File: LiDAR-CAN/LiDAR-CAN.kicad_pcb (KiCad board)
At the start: 4 copper layers, 60 x 55 mm, 137 parts, among them J1 XT30(2+2), J2 XT30(2+2), J3 G7LX-A88S7-BP-G/Y, J4 XT30(2+2), J5 61300511121, SW1 RST, U1 LMR51430, U2 LMR51430, U3 W5500, U4 TCAN4550RGY, U5 STM32F401RBT6, Y1 25MHz, Y2 40MHz, Y3 25MHz

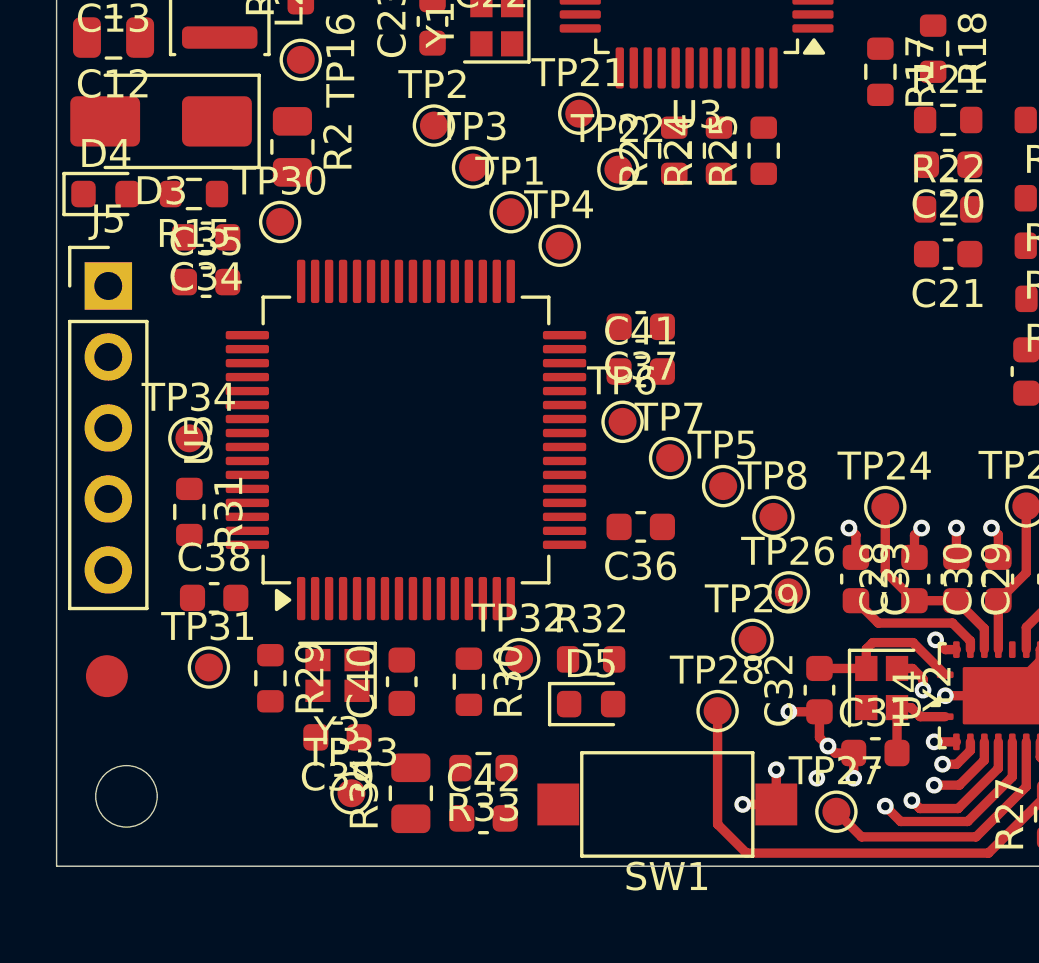
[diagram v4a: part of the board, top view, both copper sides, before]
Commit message: Add MCU routing
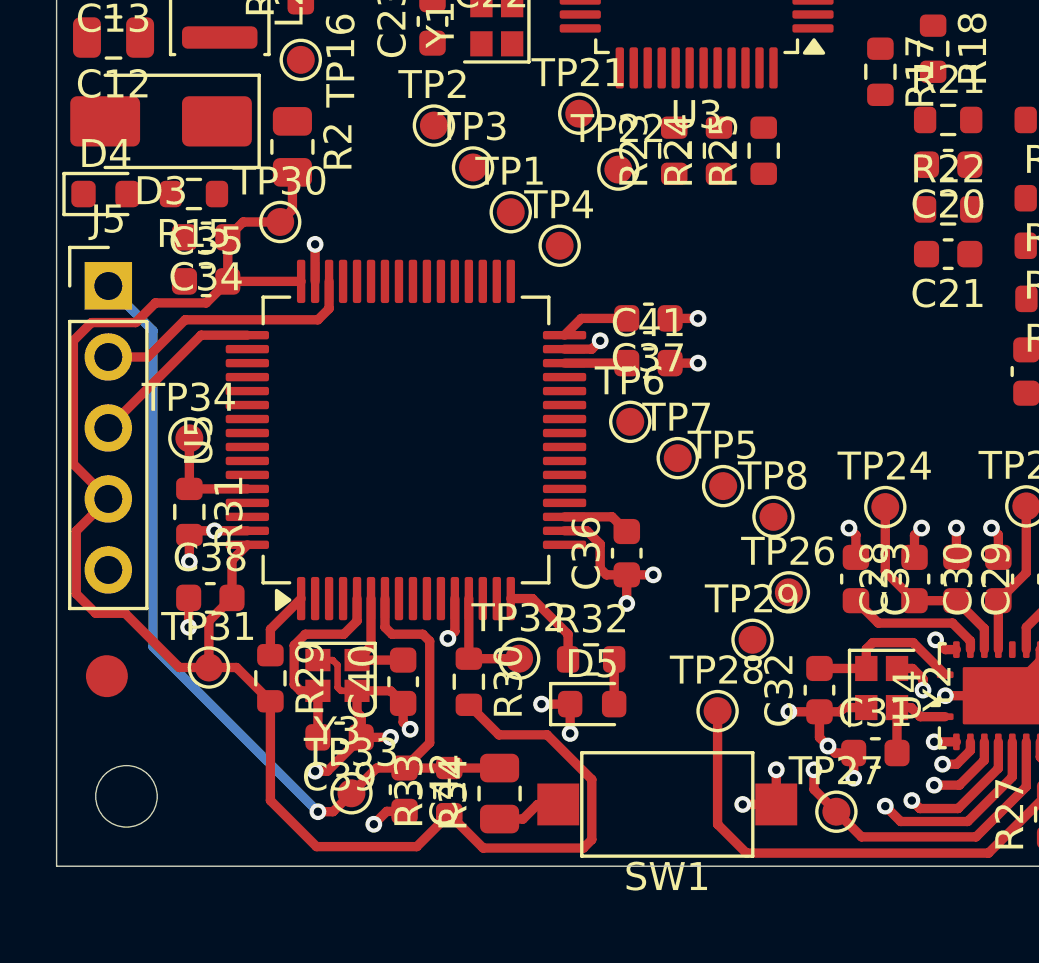
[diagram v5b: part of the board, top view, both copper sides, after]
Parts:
- moved R34 3.18 mm to (135.8, 117.4)
- moved C42 3.01 mm to (132.4, 117.3), turned to -90 degrees
- moved R33 1.48 mm to (134.1, 117.3), turned to 90 degrees
- moved C36 1.06 mm to (140.4, 108.8), turned to 90 degrees
- moved C37 0.41 mm to (141.2, 100.4)
- moved C41 0.41 mm to (141.2, 102.0)
- moved TP6 0.28 mm to (140.5, 104.1)
- moved TP7 0.28 mm to (142.2, 105.4)
- moved C38 0.14 mm to (125.5, 110.4)
- moved C39 0.07 mm to (130.1, 115.4)
- moved C40 0.05 mm to (132.4, 113.4)
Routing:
- net +3.3V: track 7.45 -> 75.1 mm
- net /Microcontroller/MCU_RST: track 0.00 -> 36.8 mm, vias 0 -> 1
- net GND: track 31.3 -> 62.0 mm, vias 17 -> 33
- net /Microcontroller/SWDIO: track 0.00 -> 9.59 mm
- net /Microcontroller/OSC_IN: track 0.00 -> 7.42 mm
- net /Microcontroller/SWCLK: track 0.00 -> 6.35 mm
- net /Microcontroller/OSC_OUT: track 0.00 -> 4.06 mm
- net /Microcontroller/VREF+: track 0.00 -> 3.95 mm
- net /Microcontroller/BOOT0: track 0.00 -> 3.89 mm
- net /Microcontroller/ULED: track 0.00 -> 3.48 mm
- net Net-(U5-VBAT): track 0.00 -> 2.48 mm
- net Net-(R34-Pad1): track 0.00 -> 2.32 mm
- net Net-(U5-VCAP1): track 0.00 -> 1.95 mm
- net /CAN Interface/~{CS}: track 9.52 -> 11.3 mm, vias 0 -> 1
- net Net-(D5-A): track 0.00 -> 1.60 mm
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
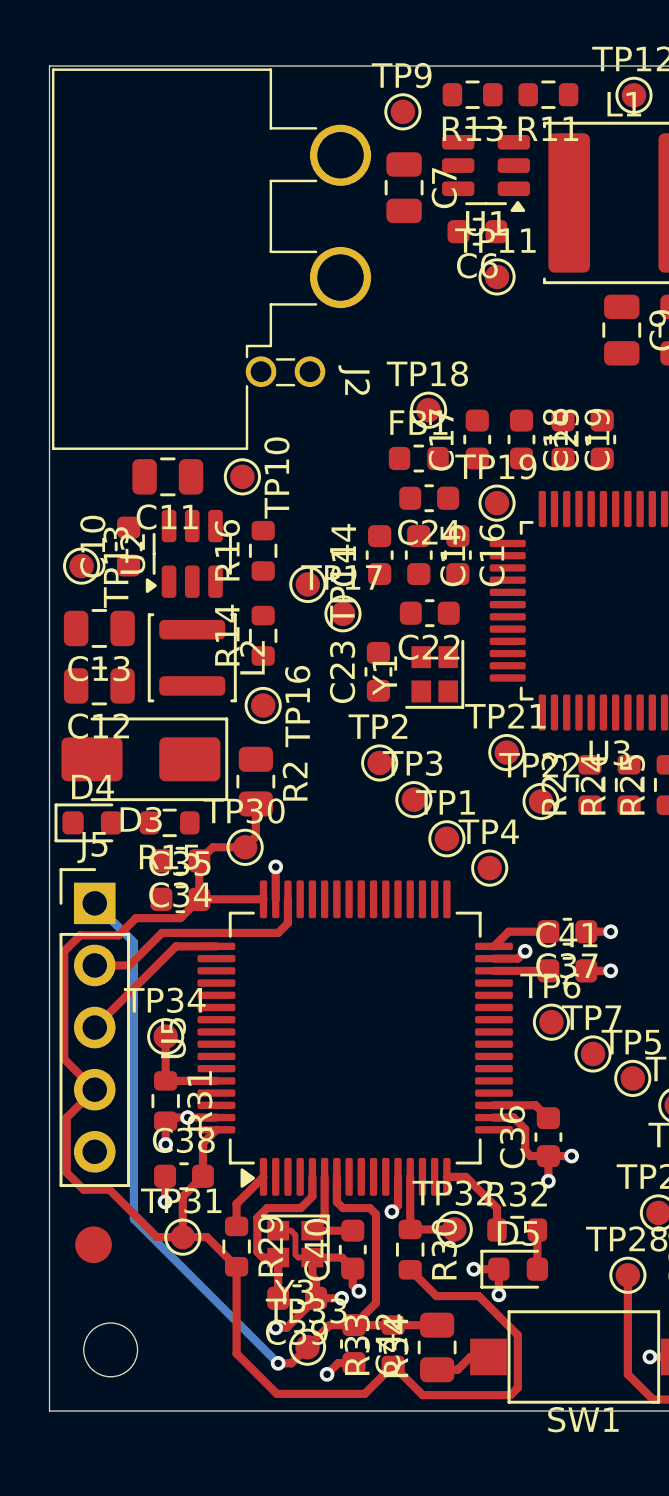
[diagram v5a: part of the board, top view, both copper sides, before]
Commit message: Add 3.3V regulator routing
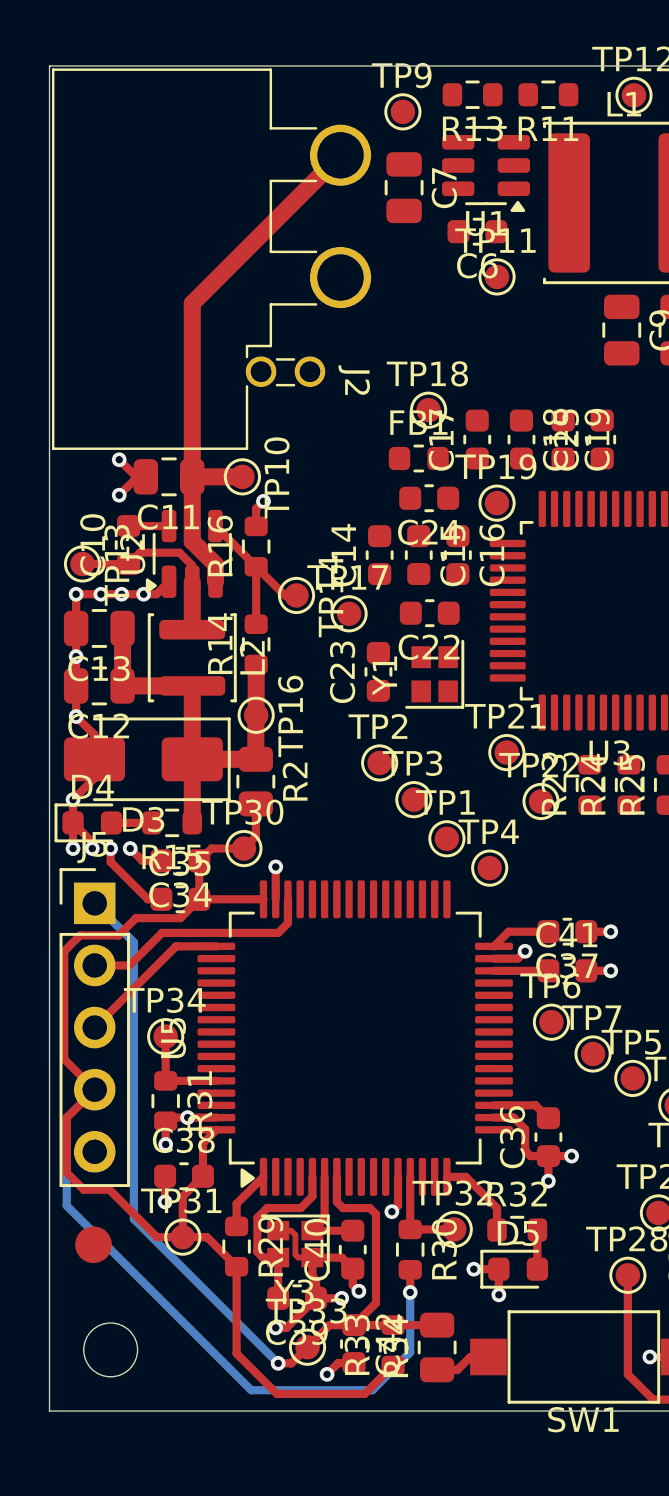
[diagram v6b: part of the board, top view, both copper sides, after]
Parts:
- moved TP14 0.65 mm to (130.1, 86.7)
- moved TP16 0.49 mm to (128.4, 91.5)
- moved R14 0.45 mm to (128.4, 88.7)
- moved R16 0.34 mm to (128.4, 84.7)
- moved TP17 0.25 mm to (132.2, 87.4)
- moved D3 0.10 mm to (123.8, 93.3)
- moved R15 0.10 mm to (125.0, 96.0)
- moved TP13 0.10 mm to (121.3, 85.4)
- moved TP30 0.07 mm to (128.0, 97.0)
- moved C10 0.06 mm to (123.2, 84.6)
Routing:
- net GND: track 62.0 -> 87.1 mm, vias 33 -> 47
- net /Power Management/VIN: track 0.00 -> 22.4 mm
- net /Power Management/3.3VOUT: track 0.00 -> 17.3 mm
- net +3.3V: track 75.1 -> 88.1 mm, vias 0 -> 1
- net /Power Management/SW_3V3: track 0.00 -> 7.52 mm
- net /Power Management/FB_3V3: track 0.00 -> 6.84 mm
- net Net-(U2-CB): track 0.00 -> 1.65 mm
- net Net-(D4-A): track 0.00 -> 1.65 mm

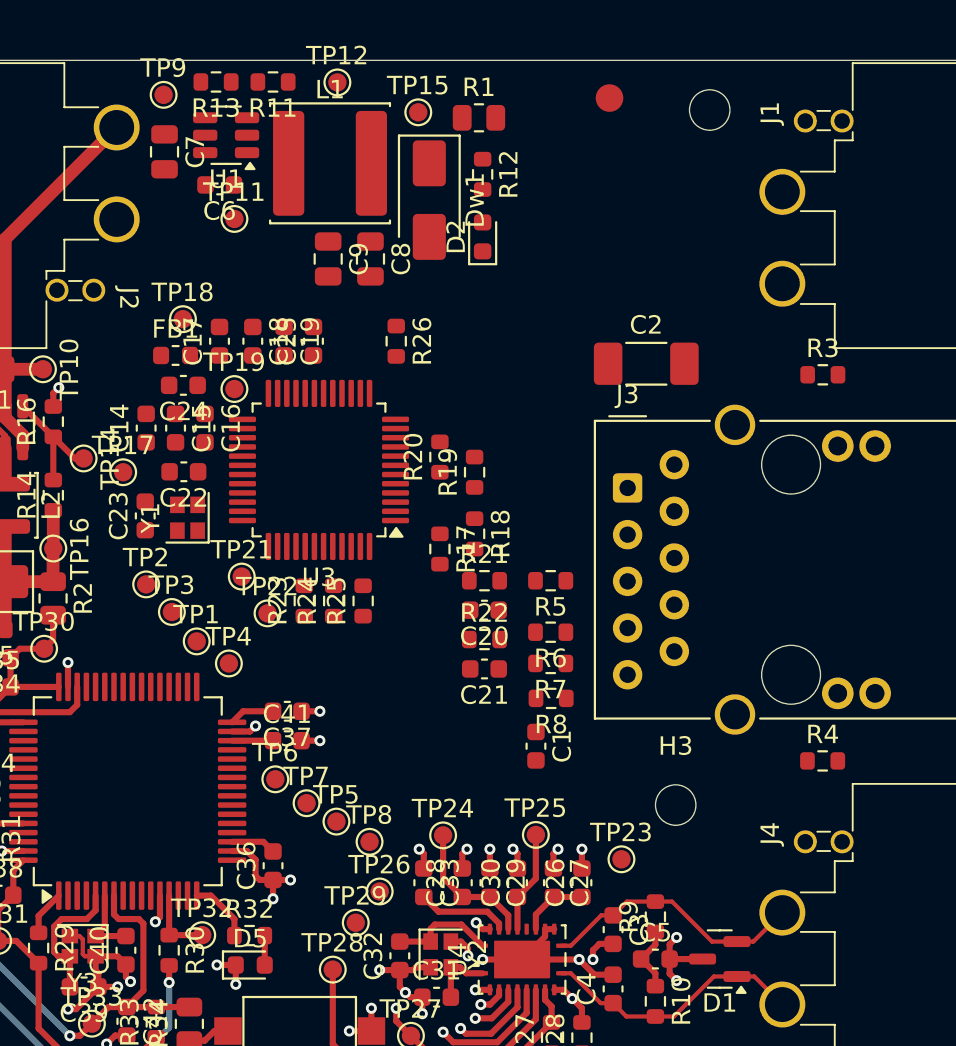
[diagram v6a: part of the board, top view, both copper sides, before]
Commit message: Add 12V regulator routing
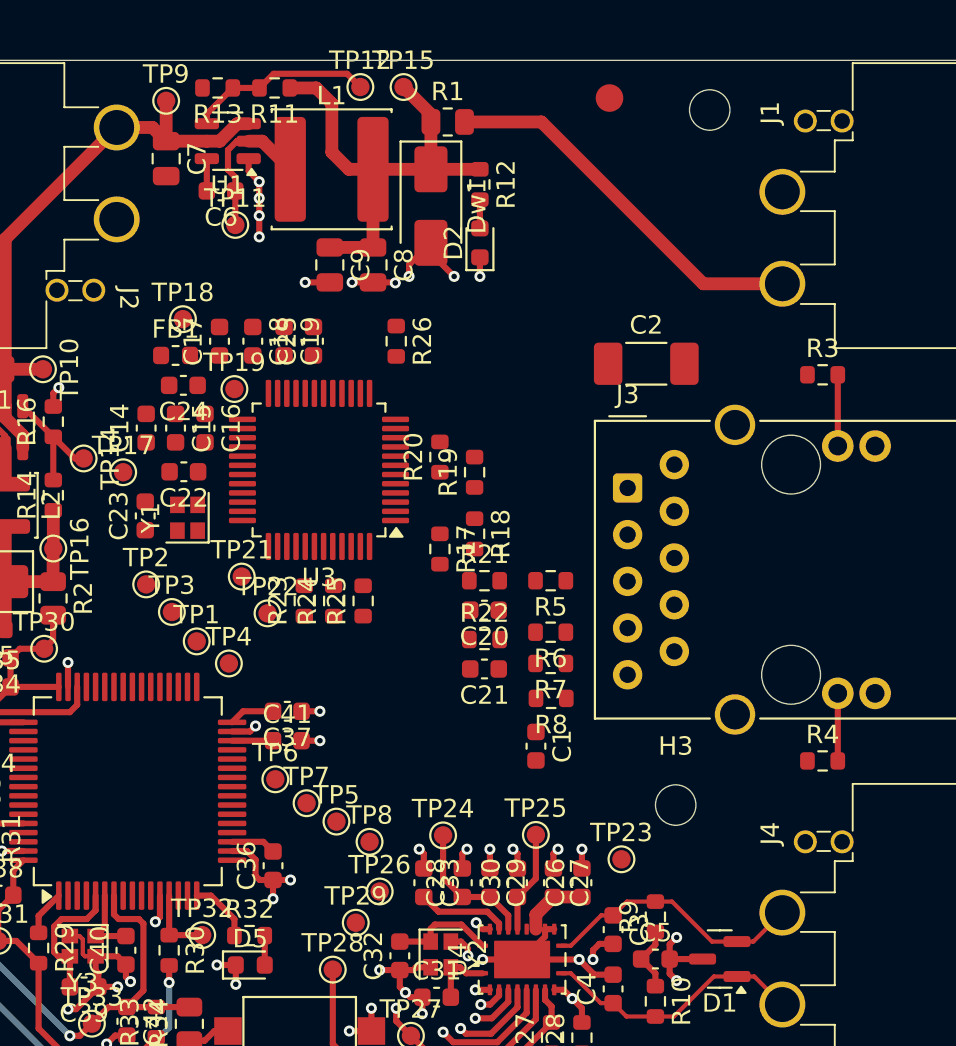
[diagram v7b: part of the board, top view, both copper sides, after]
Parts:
- moved R1 1.71 mm to (149.9, 68.3)
- moved TP15 1.59 mm to (147.5, 66.5)
- moved TP12 1.27 mm to (145.2, 66.5)
- moved R12 0.57 mm to (151.7, 71.8)
- moved C7 0.38 mm to (134.6, 70.3)
- moved D2 0.36 mm to (151.7, 74.9)
- moved C8 0.35 mm to (145.8, 76.1)
- moved TP9 0.35 mm to (134.6, 67.2)
- moved C9 0.34 mm to (143.5, 76.1)
- moved Dw1 0.34 mm to (149.0, 72.9)
- moved L1 0.34 mm to (143.6, 70.9)
- moved R11 0.34 mm to (140.5, 66.5)
- moved U1 0.34 mm to (137.9, 69.4)
- moved R13 0.34 mm to (137.4, 66.5)
- moved C6 0.33 mm to (137.6, 72.1)
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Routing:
- net /Power Management/12VOUT: track 0.00 -> 25.4 mm
- net +12V: track 3.70 -> 24.6 mm
- net GND: track 87.1 -> 101.0 mm, vias 47 -> 57
- net /Power Management/FB_12V: track 0.00 -> 10.1 mm
- net /Power Management/VIN: track 22.4 -> 32.5 mm
- net /Power Management/SW_12V: track 0.00 -> 8.46 mm
- net Net-(J3-LEDY_A): track 0.00 -> 3.88 mm
- net Net-(J3-LEDG_A): track 0.00 -> 3.67 mm
- net Net-(U1-CB): track 0.00 -> 1.75 mm
- net Net-(D2-A): track 0.00 -> 1.56 mm

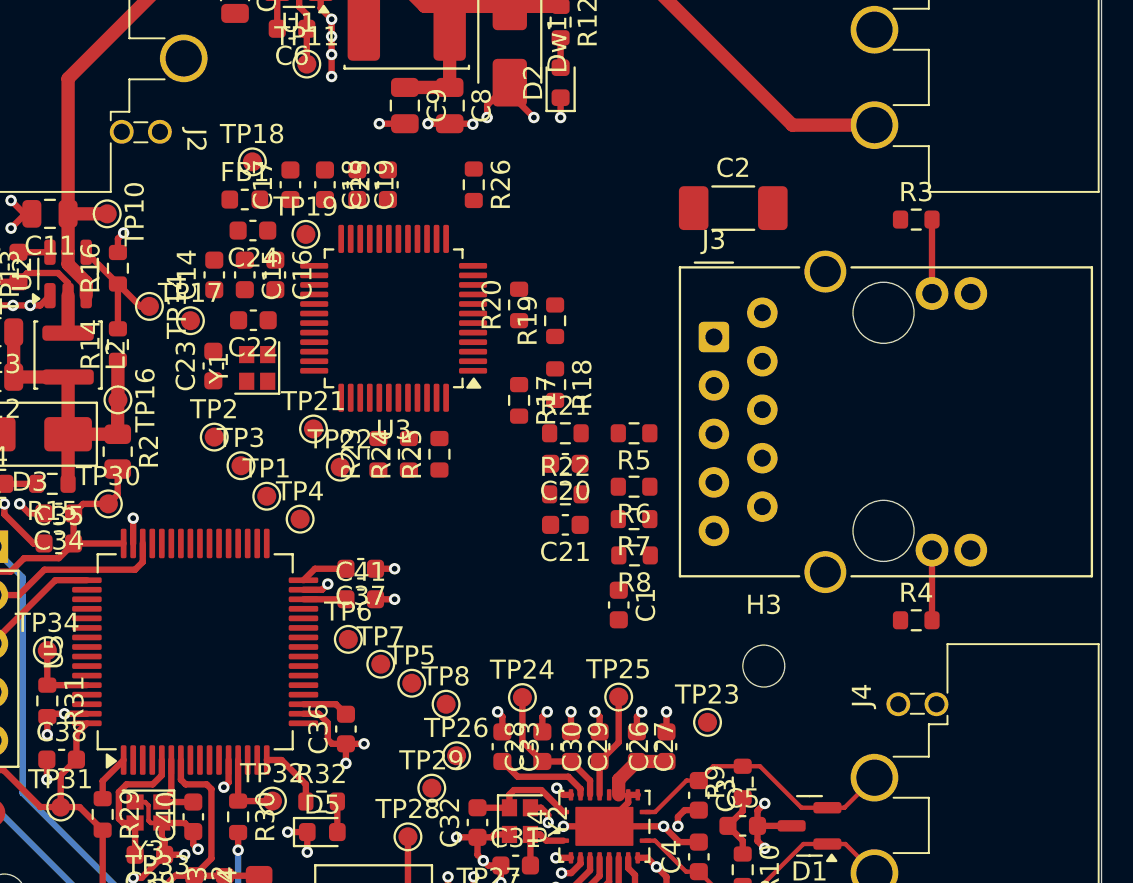
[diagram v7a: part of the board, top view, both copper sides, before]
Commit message: Add Ethernet interface routing
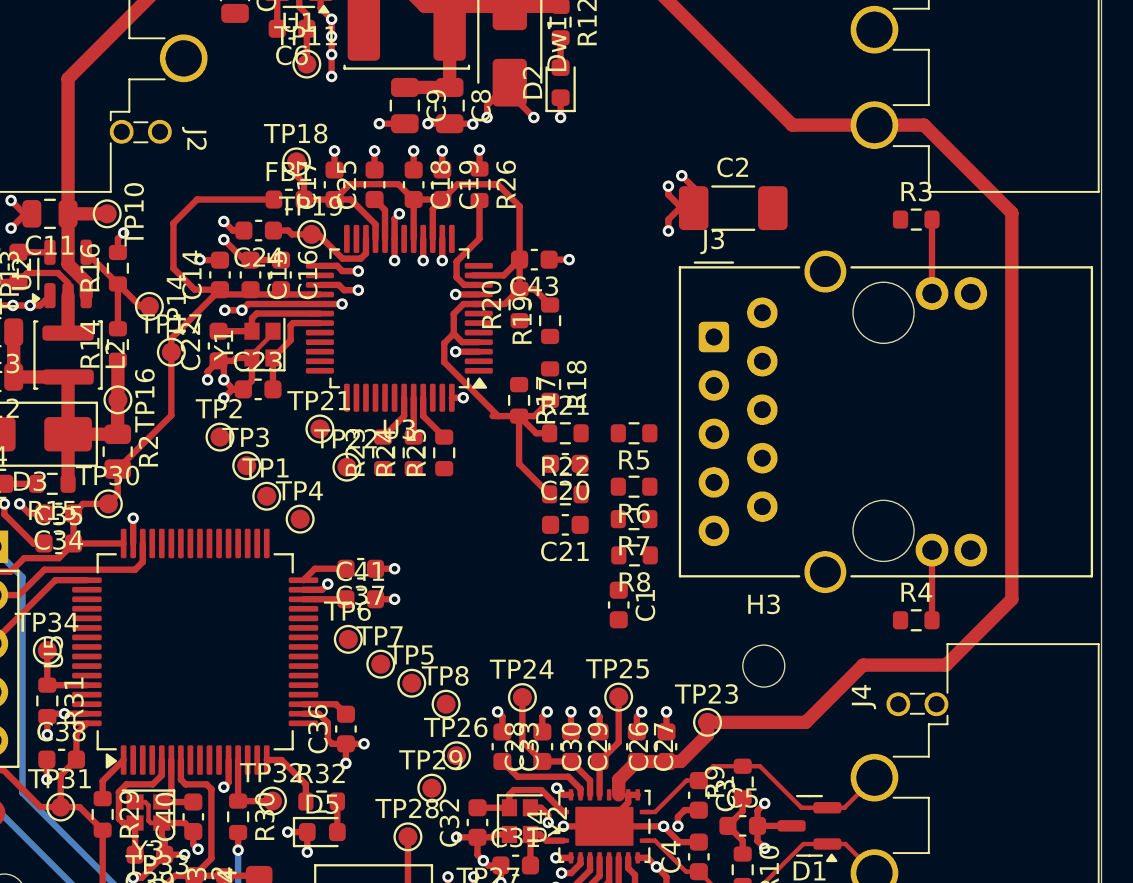
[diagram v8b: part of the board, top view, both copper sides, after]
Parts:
- added C43: 100nF, Capacitor_SMD:C_0603_1608Metric, F.Cu at (150.3, 84.2)
- moved C18 4.65 mm to (143.9, 80.3)
- moved C19 4.45 mm to (145.4, 80.3)
- moved C23 2.65 mm to (135.8, 91.0), turned to 0 degrees
- moved C17 2.31 mm to (139.8, 80.3)
- moved FB1 2.31 mm to (137.4, 81.0)
- moved TP18 2.31 mm to (137.8, 79.1)
- moved C22 2.27 mm to (133.7, 88.7), turned to 90 degrees
- moved TP17 1.93 mm to (131.2, 89.0)
- moved Y1 1.26 mm to (136.0, 88.7)
- moved C25 0.70 mm to (141.9, 80.3)
- moved TP22 0.35 mm to (140.4, 95.1)
- moved TP21 0.34 mm to (139.0, 93.1)
- moved C14 0.30 mm to (133.8, 85.0)
- moved C15 0.30 mm to (135.4, 85.0)
- moved C16 0.30 mm to (137.0, 85.0)
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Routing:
- net /LiDAR Interface/AVDD: track 0.00 -> 54.7 mm
- net +12V: track 24.6 -> 76.0 mm
- net GND: track 101.0 -> 143.2 mm, vias 57 -> 82
- net +3.3V: track 88.1 -> 115.5 mm
- net /LiDAR Interface/1V20: track 0.00 -> 6.33 mm
- net /LiDAR Interface/XI: track 0.00 -> 6.09 mm
- net /LiDAR Interface/EXRES1: track 0.00 -> 5.85 mm
- net /LiDAR Interface/XO: track 0.00 -> 5.32 mm
- net Net-(U3-PMODE0): track 0.00 -> 2.52 mm
- net Net-(U3-PMODE2): track 0.00 -> 2.52 mm
- net /LiDAR Interface/TOCAP: track 0.00 -> 2.29 mm
- net /LiDAR Interface/LINKLED: track 0.00 -> 2.13 mm, vias 0 -> 1
- net /LiDAR Interface/ACTLED: track 0.00 -> 2.13 mm, vias 0 -> 1
- net Net-(U3-PMODE1): track 0.00 -> 2.06 mm
